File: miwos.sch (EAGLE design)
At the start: 50 parts

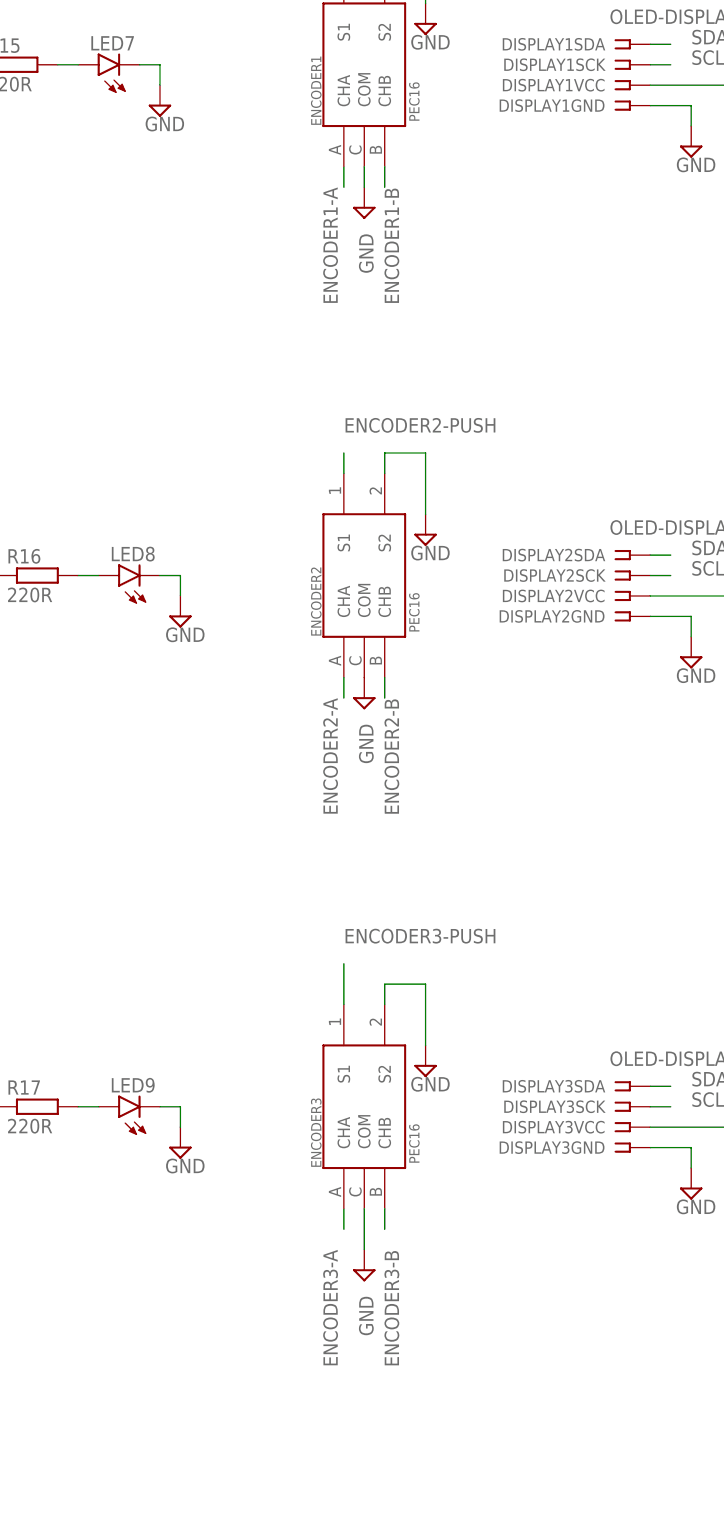
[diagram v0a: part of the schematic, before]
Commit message: Fix wrong encoder wiring
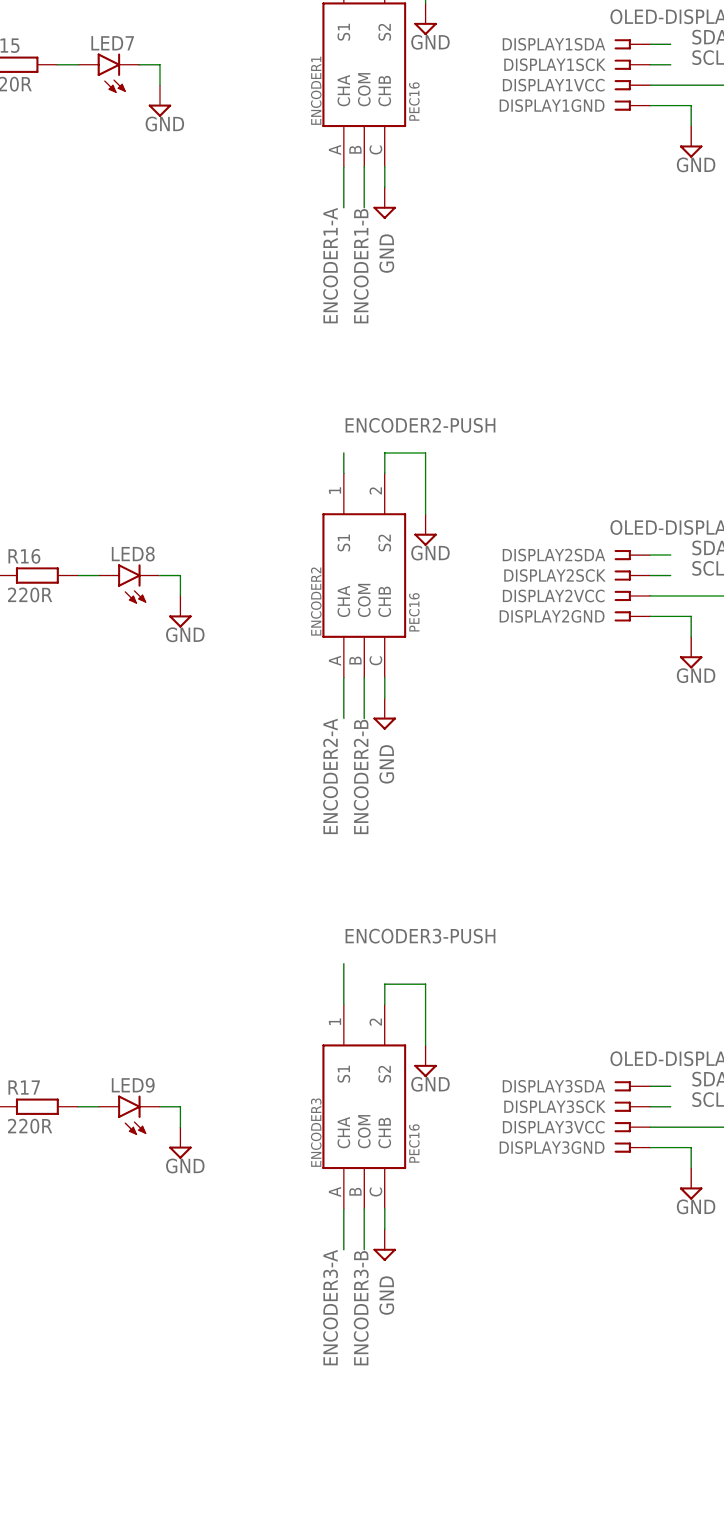
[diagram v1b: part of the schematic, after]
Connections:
- net ENCODER1-B: now also ENCODER1.COM; no longer ENCODER1.CHB
- net ENCODER2-B: now also ENCODER2.COM; no longer ENCODER2.CHB
- net ENCODER3-B: now also ENCODER3.COM; no longer ENCODER3.CHB
- net GND: now also ENCODER1.CHB, ENCODER2.CHB, ENCODER3.CHB; no longer ENCODER1.COM, ENCODER2.COM, ENCODER3.COM
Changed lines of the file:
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@@
 <setting verticaltext="up"/>
 </settings>
-<grid distance="0.1" unitdist="inch" unit="inch" style="lines" multiple="1" display="no" altdistance="0.01" altunitdist="inch" altunit="inch"/>
+<grid distance="0.1" unitdist="inch" unit="inch" style="lines" multiple="1" display="no" altdistance="0.05" altunitdist="inch" altunit="inch"/>
 <layers>
 <layer number="1" name="Top" color="4" fill="1" visible="no" active="no"/>
@@
 <attribute name="VALUE" x="-76.96176875" y="112.267759375" size="1.270040625" layer="96" rot="R90"/>
 </instance>
-<instance part="SUPPLY1" gate="GND" x="-83.82" y="101.6" smashed="yes">
-<attribute name="VALUE" x="-84.455" y="98.425" size="1.778" layer="96" rot="R270"/>
+<instance part="SUPPLY1" gate="GND" x="-81.28" y="101.6" smashed="yes">
+<attribute name="VALUE" x="-81.915" y="98.425" size="1.778" layer="96" rot="R270"/>
 </instance>
 <instance part="TEENSY-41" gate="G$2" x="106.68" y="-5.08" smashed="yes" rot="R180">
@@
 <attribute name="VALUE" x="-76.96176875" y="48.767759375" size="1.270040625" layer="96" rot="R90"/>
 </instance>
-<instance part="SUPPLY3" gate="GND" x="-83.82" y="40.64" smashed="yes">
-<attribute name="VALUE" x="-84.455" y="37.465" size="1.778" layer="96" rot="R270"/>
+<instance part="SUPPLY3" gate="GND" x="-81.28" y="38.1" smashed="yes">
+<attribute name="VALUE" x="-81.915" y="34.925" size="1.778" layer="96" rot="R270"/>
 </instance>
 <instance part="SUPPLY4" gate="GND" x="-76.2" y="60.96" smashed="yes">
@@
 <attribute name="VALUE" x="-76.96176875" y="-17.272240625" size="1.270040625" layer="96" rot="R90"/>
 </instance>
-<instance part="SUPPLY5" gate="GND" x="-83.82" y="-30.48" smashed="yes">
-<attribute name="VALUE" x="-84.455" y="-33.655" size="1.778" layer="96" rot="R270"/>
+<instance part="SUPPLY5" gate="GND" x="-81.28" y="-27.94" smashed="yes">
+<attribute name="VALUE" x="-81.915" y="-31.115" size="1.778" layer="96" rot="R270"/>
 </instance>
 <instance part="SUPPLY6" gate="GND" x="-76.2" y="-5.08" smashed="yes">
@@
 <net name="GND" class="0">
 <segment>
-<pinref part="SUPPLY1" gate="GND" pin="GND"/>
-<pinref part="ENCODER1" gate="G$1" pin="COM"/>
-<wire x1="-83.82" y1="104.14" x2="-83.82" y2="106.68" width="0.1524" layer="91"/>
-</segment>
-<segment>
 <pinref part="ENCODER1" gate="G$1" pin="S2"/>
 <pinref part="SUPPLY2" gate="GND" pin="GND"/>
@@
 </segment>
 <segment>
-<pinref part="SUPPLY3" gate="GND" pin="GND"/>
-<pinref part="ENCODER2" gate="G$1" pin="COM"/>
-</segment>
-<segment>
 <pinref part="ENCODER2" gate="G$1" pin="S2"/>
 <pinref part="SUPPLY4" gate="GND" pin="GND"/>
@@
 <wire x1="-81.28" y1="71.12" x2="-76.2" y2="71.12" width="0.1524" layer="91"/>
 <wire x1="-76.2" y1="71.12" x2="-76.2" y2="63.5" width="0.1524" layer="91"/>
-</segment>
-<segment>
-<pinref part="SUPPLY5" gate="GND" pin="GND"/>
-<pinref part="ENCODER3" gate="G$1" pin="COM"/>
-<wire x1="-83.82" y1="-27.94" x2="-83.82" y2="-22.86" width="0.1524" layer="91"/>
 </segment>
 <segment>
@@
 <wire x1="-106.68" y1="-10.16" x2="-106.68" y2="-12.7" width="0.1524" layer="91"/>
 </segment>
+<segment>
+<pinref part="ENCODER1" gate="G$1" pin="CHB"/>
+<pinref part="SUPPLY1" gate="GND" pin="GND"/>
+<wire x1="-81.28" y1="104.14" x2="-81.28" y2="106.68" width="0.1524" layer="91"/>
+</segment>
+<segment>
+<pinref part="ENCODER2" gate="G$1" pin="CHB"/>
+<pinref part="SUPPLY3" gate="GND" pin="GND"/>
+<wire x1="-81.28" y1="43.18" x2="-81.28" y2="40.64" width="0.1524" layer="91"/>
+</segment>
+<segment>
+<pinref part="ENCODER3" gate="G$1" pin="CHB"/>
+<wire x1="-81.28" y1="-22.86" x2="-81.28" y2="-25.4" width="0.1524" layer="91"/>
+<pinref part="SUPPLY5" gate="GND" pin="GND"/>
+</segment>
 </net>
 <net name="ENCODER2-A" class="0">
 <segment>
 <pinref part="ENCODER2" gate="G$1" pin="CHA"/>
-<wire x1="-86.36" y1="40.64" x2="-86.36" y2="43.18" width="0.1524" layer="91"/>
-<label x="-88.9" y="40.64" size="1.778" layer="95" rot="R270"/>
+<wire x1="-86.36" y1="38.1" x2="-86.36" y2="43.18" width="0.1524" layer="91"/>
+<label x="-88.9" y="38.1" size="1.778" layer="95" rot="R270"/>
 </segment>
 <segment>
@@
 <net name="ENCODER3-B" class="0">
 <segment>
-<pinref part="ENCODER3" gate="G$1" pin="CHB"/>
-<wire x1="-81.28" y1="-22.86" x2="-81.28" y2="-25.4" width="0.1524" layer="91"/>
-<label x="-81.28" y="-27.94" size="1.778" layer="95" rot="R270"/>
-</segment>
-<segment>
 <pinref part="TEENSY-41" gate="G$1" pin="33"/>
 <wire x1="43.18" y1="33.02" x2="48.26" y2="33.02" width="0.1524" layer="91"/>
 <label x="50.8" y="33.02" size="1.778" layer="95"/>
+</segment>
+<segment>
+<pinref part="ENCODER3" gate="G$1" pin="COM"/>
+<wire x1="-83.82" y1="-22.86" x2="-83.82" y2="-27.94" width="0.1524" layer="91"/>
+<label x="-85.09" y="-27.94" size="1.778" layer="95" rot="R270"/>
 </segment>
 </net>
@@
 <net name="ENCODER2-B" class="0">
 <segment>
-<pinref part="ENCODER2" gate="G$1" pin="CHB"/>
-<wire x1="-81.28" y1="43.18" x2="-81.28" y2="40.64" width="0.1524" layer="91"/>
-<label x="-81.28" y="40.64" size="1.778" layer="95" rot="R270"/>
-</segment>
-<segment>
 <pinref part="TEENSY-41" gate="G$1" pin="36"/>
 <wire x1="43.18" y1="40.64" x2="48.26" y2="40.64" width="0.1524" layer="91"/>
 <label x="50.8" y="40.64" size="1.778" layer="95"/>
 </segment>
+<segment>
+<pinref part="ENCODER2" gate="G$1" pin="COM"/>
+<wire x1="-83.82" y1="43.18" x2="-83.82" y2="38.1" width="0.1524" layer="91"/>
+<label x="-85.09" y="38.1" size="1.778" layer="95" rot="R270"/>
+</segment>
 </net>
 <net name="ENCODER2-PUSH" class="0">
@@
 <segment>
 <pinref part="ENCODER3" gate="G$1" pin="CHA"/>
-<wire x1="-86.36" y1="-22.86" x2="-86.36" y2="-25.4" width="0.1524" layer="91"/>
+<wire x1="-86.36" y1="-22.86" x2="-86.36" y2="-27.94" width="0.1524" layer="91"/>
 <label x="-88.9" y="-27.94" size="1.778" layer="95" rot="R270"/>
 </segment>
@@
 <segment>
 <pinref part="ENCODER1" gate="G$1" pin="CHA"/>
-<wire x1="-86.36" y1="106.68" x2="-86.36" y2="104.14" width="0.1524" layer="91"/>
-<label x="-88.9" y="104.14" size="1.778" layer="95" rot="R270"/>
+<wire x1="-86.36" y1="106.68" x2="-86.36" y2="101.6" width="0.1524" layer="91"/>
+<label x="-88.9" y="101.6" size="1.778" layer="95" rot="R270"/>
 </segment>
 </net>
@@
 </segment>
 <segment>
-<pinref part="ENCODER1" gate="G$1" pin="CHB"/>
-<wire x1="-81.28" y1="106.68" x2="-81.28" y2="104.14" width="0.1524" layer="91"/>
-<label x="-81.28" y="104.14" size="1.778" layer="95" rot="R270"/>
-</segment>
-</net>
+<pinref part="ENCODER1" gate="G$1" pin="COM"/>
+<wire x1="-83.82" y1="106.68" x2="-83.82" y2="101.6" width="0.1524" layer="91"/>
+<label x="-85.09" y="101.6" size="1.778" layer="95" rot="R270"/>
+</segment>
+</net>

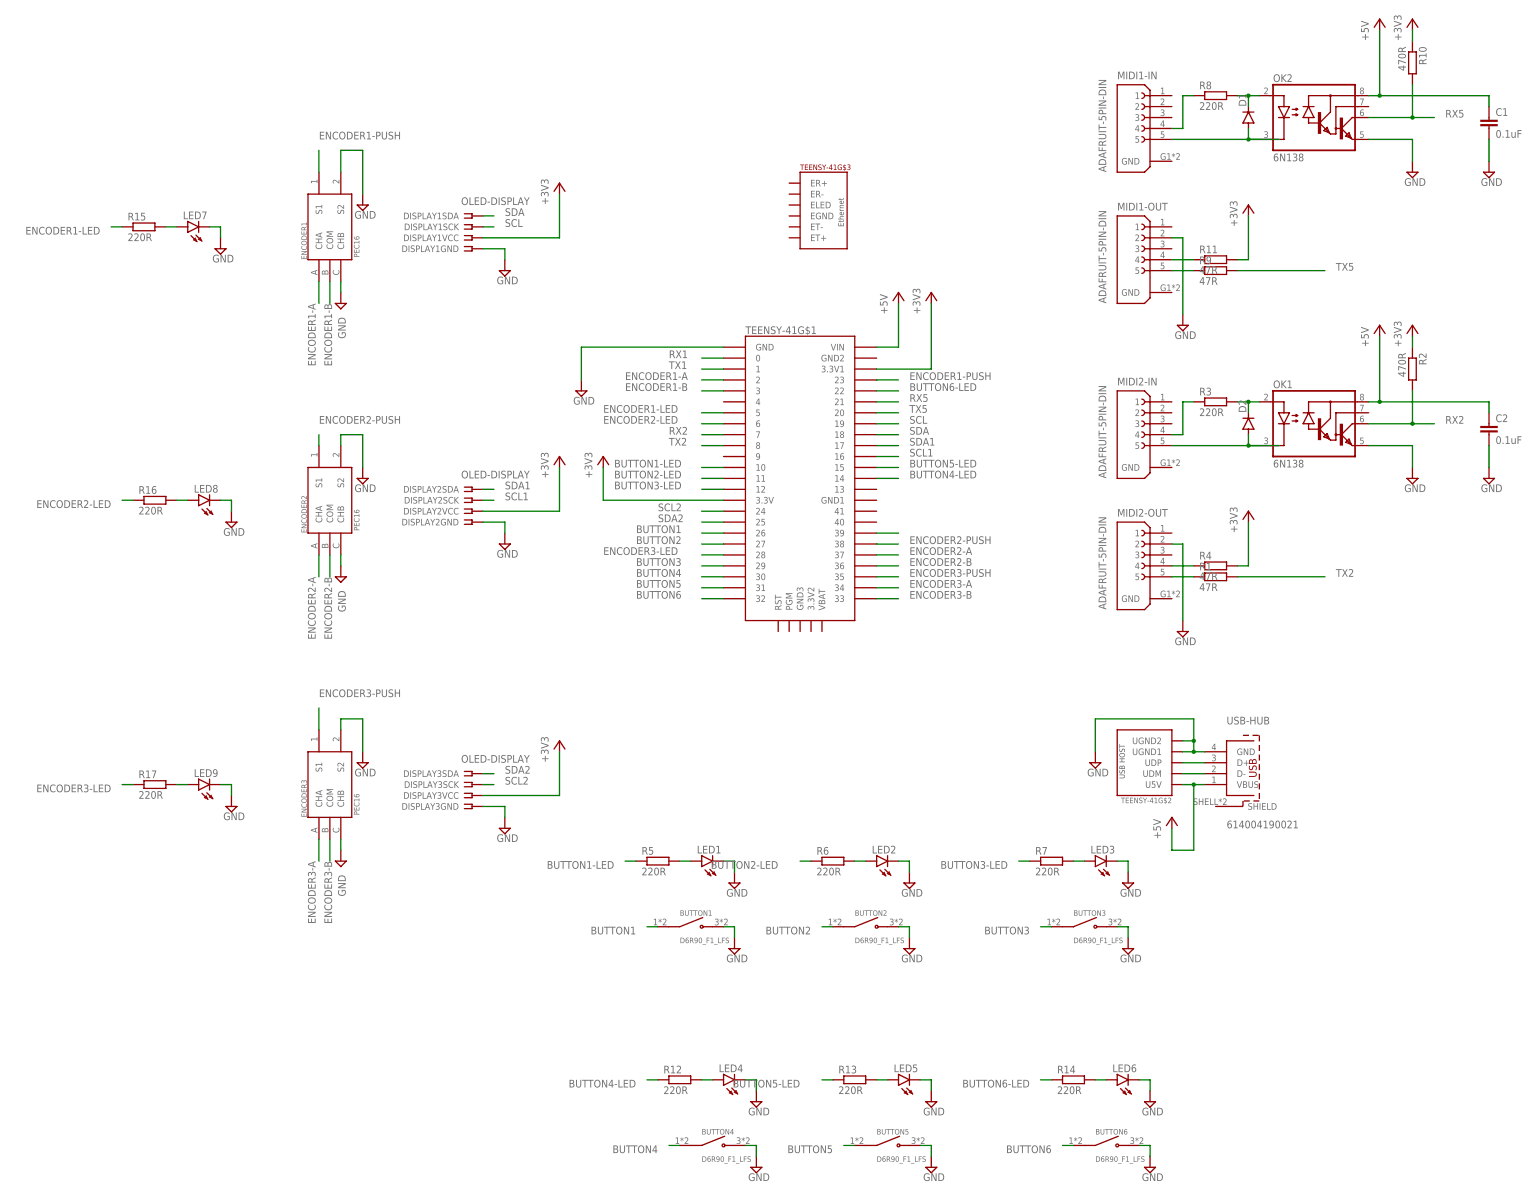
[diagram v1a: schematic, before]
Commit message: Update to illuminated D6R buttons
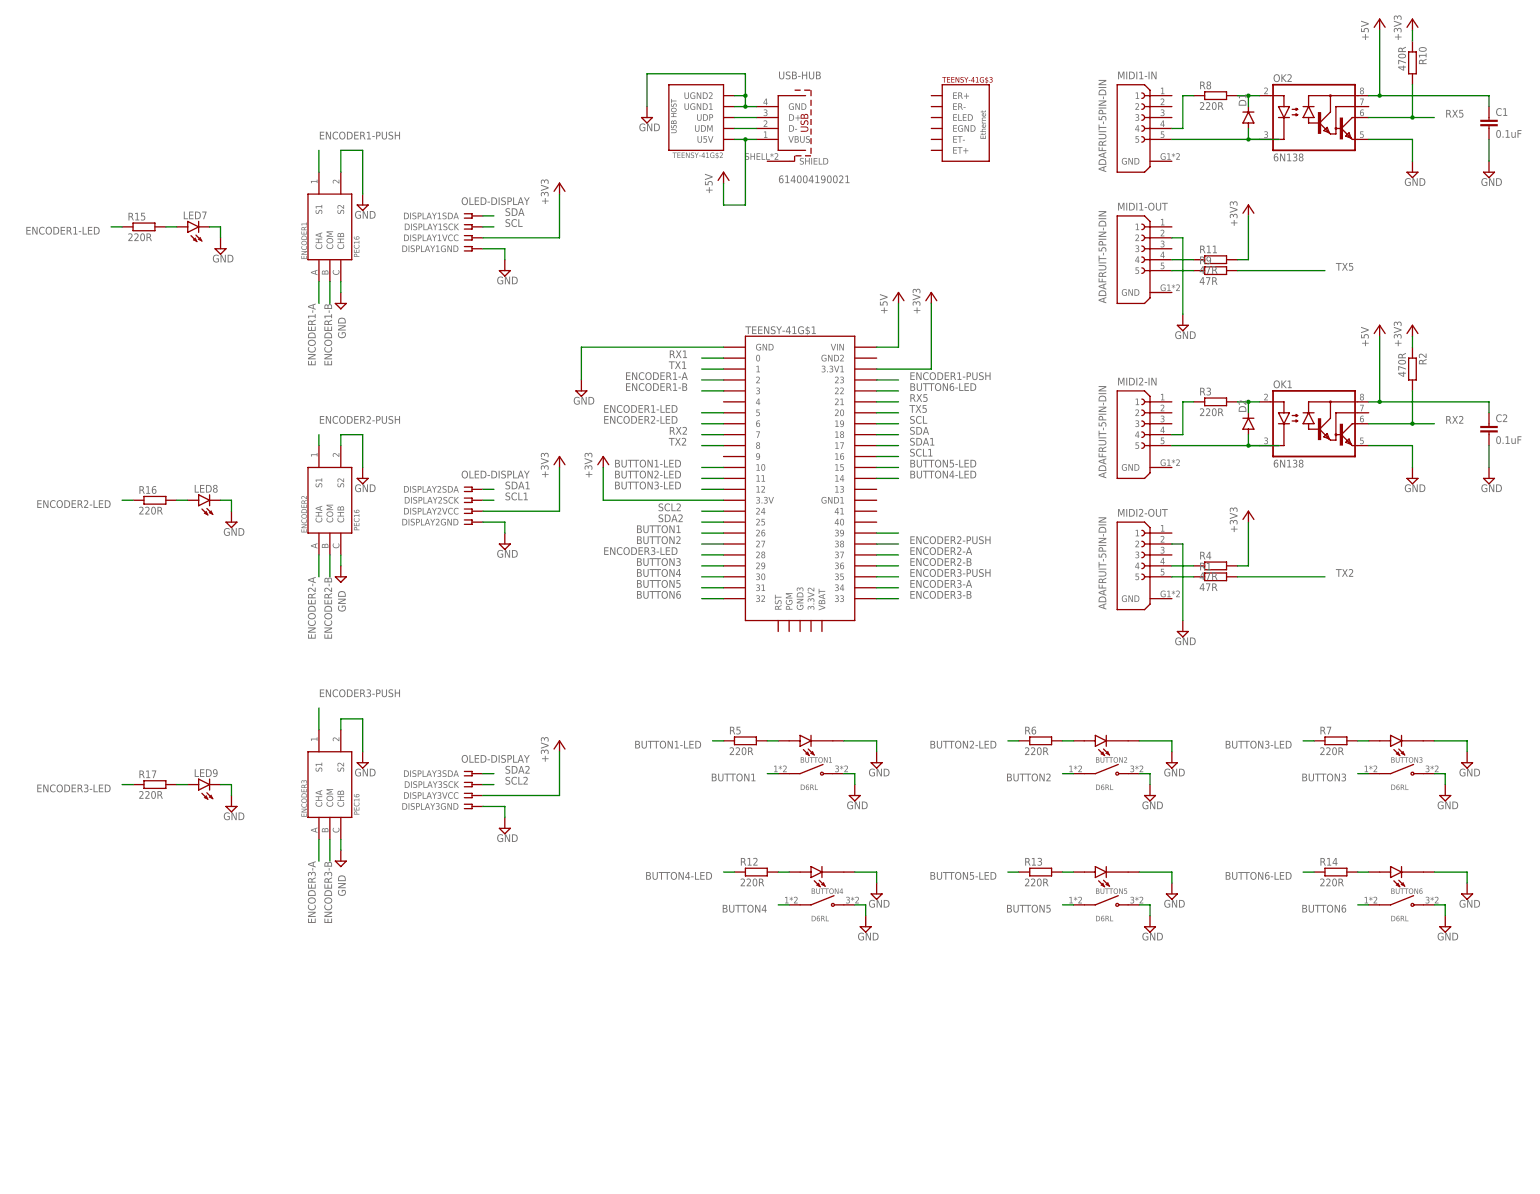
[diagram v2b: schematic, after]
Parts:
- removed LED1, LED2, LED3, LED4, LED5, LED6: (no value), led:LED3MM
- BUTTON1, BUTTON2, BUTTON3, BUTTON4, BUTTON5, BUTTON6: value D6R90_F1_LFS -> D6RL; device D6R90_F1_LFS:D6R90_F1_LFS -> D6RL:D6RL
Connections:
- removed net N$7: LED3.A, R7.2
- new net N$23: BUTTON5.LED, R13.2
- net GND: now also BUTTON1.COM-LED, BUTTON2.COM-LED, BUTTON3.COM-LED, BUTTON4.COM-LED, BUTTON5.COM-LED, BUTTON6.COM-LED; no longer LED1.C, LED2.C, LED3.C, LED4.C, LED5.C, LED6.C
- net N$13: now also BUTTON4.LED; no longer LED4.A
- net N$14: now also BUTTON1.LED, R5.2; no longer LED5.A, R13.2
- net N$15: now also BUTTON6.LED; no longer LED6.A
- net N$5: now also BUTTON3.LED, R7.2; no longer LED1.A, R5.2
- net N$6: now also BUTTON2.LED; no longer LED2.A
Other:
- moved on the sheet: R12, R13, R14, R5, R6, R7, TEENSY-41G$2, TEENSY-41G$3, USB-HUB
